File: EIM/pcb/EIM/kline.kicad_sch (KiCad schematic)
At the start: 8 parts, among them IC1 TLIN1027DRQ1

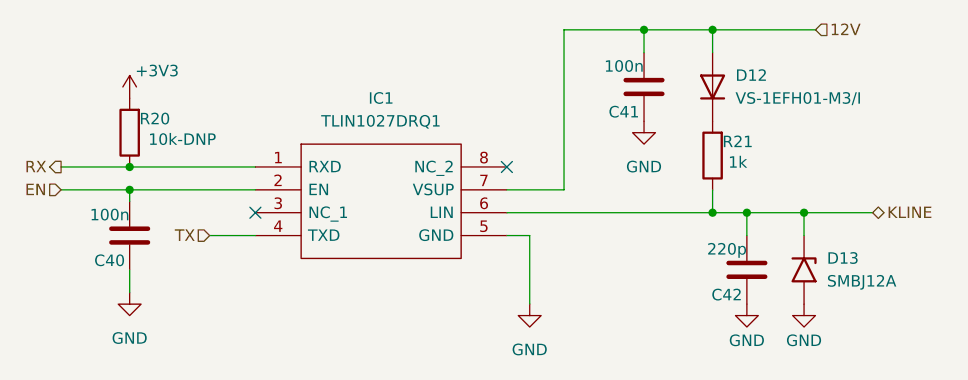
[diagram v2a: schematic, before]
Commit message: All components placed and pins assigned.
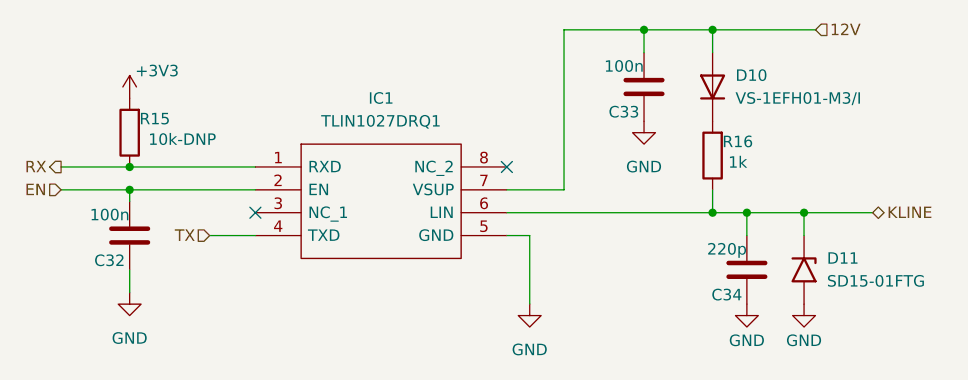
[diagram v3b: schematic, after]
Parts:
- removed D13: SMBJ12A, Diode_SMD:D_SMB, symbol Diode:SM6T10A
- added D11: SD15-01FTG, Diode_SMD:D_SOD-323, symbol Diode:SM6T10A
- renumbered C40 to C32, C41 to C33, C42 to C34, D12 to D10, R20 to R15, R21 to R16
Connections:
- net GND: now also D11.2 (A2)
- net KLINE: now also D11.1 (A1)
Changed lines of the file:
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@@
 		(on_board yes)
 		(dnp no)
-		(property "Reference" "#PWR093"
+		(property "Reference" "#PWR086"
 			(at 186.69 113.03 0)
 			(effects
@@
 			(project "EIM"
 				(path "/2e0b3b3d-5537-41dc-9fad-4fb33afdbfad/08df7d8f-6781-4b98-a316-f1c5c896db59"
-					(reference "#PWR093")
+					(reference "#PWR086")
 					(unit 1)
 				)
@@
 		(dnp no)
 		(fields_autoplaced yes)
-		(property "Reference" "#PWR091"
+		(property "Reference" "#PWR084"
 			(at 162.56 113.03 0)
 			(effects
@@
 			(project ""
 				(path "/2e0b3b3d-5537-41dc-9fad-4fb33afdbfad/08df7d8f-6781-4b98-a316-f1c5c896db59"
-					(reference "#PWR091")
+					(reference "#PWR084")
 					(unit 1)
 				)
@@
 		(on_board yes)
 		(dnp no)
-		(property "Reference" "#PWR089"
+		(property "Reference" "#PWR082"
 			(at 118.11 87.63 0)
 			(effects
@@
 			(project "EIM"
 				(path "/2e0b3b3d-5537-41dc-9fad-4fb33afdbfad/08df7d8f-6781-4b98-a316-f1c5c896db59"
-					(reference "#PWR089")
+					(reference "#PWR082")
 					(unit 1)
 				)
@@
 		(on_board yes)
 		(dnp no)
-		(property "Reference" "C41"
+		(property "Reference" "C33"
 			(at 174.752 85.344 0)
 			(effects
@@
 			(project "EIM"
 				(path "/2e0b3b3d-5537-41dc-9fad-4fb33afdbfad/08df7d8f-6781-4b98-a316-f1c5c896db59"
-					(reference "C41")
+					(reference "C33")
 					(unit 1)
 				)
@@
 		(dnp no)
 		(fields_autoplaced yes)
-		(property "Reference" "#PWR090"
+		(property "Reference" "#PWR083"
 			(at 118.11 111.76 0)
 			(effects
@@
 			(project "EIM"
 				(path "/2e0b3b3d-5537-41dc-9fad-4fb33afdbfad/08df7d8f-6781-4b98-a316-f1c5c896db59"
-					(reference "#PWR090")
+					(reference "#PWR083")
+					(unit 1)
+				)
+			)
+		)
+	)
+	(symbol
+		(lib_id "Diode:SM6T10A")
+		(at 193.04 102.87 270)
+		(unit 1)
+		(exclude_from_sim no)
+		(in_bom yes)
+		(on_board yes)
+		(dnp no)
+		(property "Reference" "D11"
+			(at 195.58 101.5999 90)
+			(effects
+				(font
+					(size 1.27 1.27)
+				)
+				(justify left)
+			)
+		)
+		(property "Value" "SD15-01FTG"
+			(at 195.58 104.1399 90)
+			(effects
+				(font
+					(size 1.27 1.27)
+				)
+				(justify left)
+			)
+		)
+		(property "Footprint" "Diode_SMD:D_SOD-323"
+			(at 187.96 102.87 0)
+			(effects
+				(font
+					(size 1.27 1.27)
+				)
+				(hide yes)
+			)
+		)
+		(property "Datasheet" "https://www.st.com/resource/en/datasheet/sm6t.pdf"
+			(at 193.04 101.6 0)
+			(effects
+				(font
+					(size 1.27 1.27)
+				)
+				(hide yes)
+			)
+		)
+		(property "Description" "600W unidirectional Transil Transient Voltage Suppressor, 10Vrwm, DO-214AA"
+			(at 193.04 102.87 0)
+			(effects
+				(font
+					(size 1.27 1.27)
+				)
+				(hide yes)
+			)
+		)
+		(pin "1"
+		)
+		(pin "2"
+		)
+		(instances
+			(project "EIM"
+				(path "/2e0b3b3d-5537-41dc-9fad-4fb33afdbfad/08df7d8f-6781-4b98-a316-f1c5c896db59"
+					(reference "D11")
 					(unit 1)
 				)
@@
 		(on_board yes)
 		(dnp no)
-		(property "Reference" "C42"
+		(property "Reference" "C34"
 			(at 186.182 105.664 0)
 			(effects
@@
 			(project "EIM"
 				(path "/2e0b3b3d-5537-41dc-9fad-4fb33afdbfad/08df7d8f-6781-4b98-a316-f1c5c896db59"
-					(reference "C42")
-					(unit 1)
-				)
-			)
-		)
-	)
-	(symbol
-		(lib_id "Diode:SM6T10A")
-		(at 193.04 102.87 270)
-		(unit 1)
-		(exclude_from_sim no)
-		(in_bom yes)
-		(on_board yes)
-		(dnp no)
-		(property "Reference" "D13"
-			(at 195.58 101.5999 90)
-			(effects
-				(font
-					(size 1.27 1.27)
-				)
-				(justify left)
-			)
-		)
-		(property "Value" "SMBJ12A"
-			(at 195.58 104.1399 90)
-			(effects
-				(font
-					(size 1.27 1.27)
-				)
-				(justify left)
-			)
-		)
-		(property "Footprint" "Diode_SMD:D_SMB"
-			(at 187.96 102.87 0)
-			(effects
-				(font
-					(size 1.27 1.27)
-				)
-				(hide yes)
-			)
-		)
-		(property "Datasheet" "https://www.st.com/resource/en/datasheet/sm6t.pdf"
-			(at 193.04 101.6 0)
-			(effects
-				(font
-					(size 1.27 1.27)
-				)
-				(hide yes)
-			)
-		)
-		(property "Description" "600W unidirectional Transil Transient Voltage Suppressor, 10Vrwm, DO-214AA"
-			(at 193.04 102.87 0)
-			(effects
-				(font
-					(size 1.27 1.27)
-				)
-				(hide yes)
-			)
-		)
-		(pin "1"
-		)
-		(pin "2"
-		)
-		(instances
-			(project "EIM"
-				(path "/2e0b3b3d-5537-41dc-9fad-4fb33afdbfad/08df7d8f-6781-4b98-a316-f1c5c896db59"
-					(reference "D13")
+					(reference "C34")
 					(unit 1)
 				)
@@
 		(on_board yes)
 		(dnp no)
-		(property "Reference" "R21"
+		(property "Reference" "R16"
 			(at 185.674 88.646 0)
 			(effects
@@
 			(project "EIM"
 				(path "/2e0b3b3d-5537-41dc-9fad-4fb33afdbfad/08df7d8f-6781-4b98-a316-f1c5c896db59"
-					(reference "R21")
+					(reference "R16")
 					(unit 1)
 				)
@@
 		(dnp no)
 		(fields_autoplaced yes)
-		(property "Reference" "D12"
+		(property "Reference" "D10"
 			(at 185.42 81.2799 90)
 			(effects
@@
 			(project ""
 				(path "/2e0b3b3d-5537-41dc-9fad-4fb33afdbfad/08df7d8f-6781-4b98-a316-f1c5c896db59"
-					(reference "D12")
+					(reference "D10")
 					(unit 1)
 				)
@@
 		(on_board yes)
 		(dnp no)
-		(property "Reference" "#PWR094"
+		(property "Reference" "#PWR087"
 			(at 193.04 113.03 0)
 			(effects
@@
 			(project "EIM"
 				(path "/2e0b3b3d-5537-41dc-9fad-4fb33afdbfad/08df7d8f-6781-4b98-a316-f1c5c896db59"
-					(reference "#PWR094")
+					(reference "#PWR087")
 					(unit 1)
 				)
@@
 		(dnp no)
 		(fields_autoplaced yes)
-		(property "Reference" "#PWR092"
+		(property "Reference" "#PWR085"
 			(at 175.26 92.71 0)
 			(effects
@@
 			(project "EIM"
 				(path "/2e0b3b3d-5537-41dc-9fad-4fb33afdbfad/08df7d8f-6781-4b98-a316-f1c5c896db59"
-					(reference "#PWR092")
+					(reference "#PWR085")
 					(unit 1)
 				)
@@
 		(on_board yes)
 		(dnp no)
-		(property "Reference" "C40"
+		(property "Reference" "C32"
 			(at 117.602 101.854 0)
 			(effects
@@
 			(project "EIM"
 				(path "/2e0b3b3d-5537-41dc-9fad-4fb33afdbfad/08df7d8f-6781-4b98-a316-f1c5c896db59"
-					(reference "C40")
+					(reference "C32")
 					(unit 1)
 				)
@@
 		(on_board yes)
 		(dnp no)
-		(property "Reference" "R20"
+		(property "Reference" "R15"
 			(at 120.904 86.106 0)
 			(effects
@@
 			(project "EIM"
 				(path "/2e0b3b3d-5537-41dc-9fad-4fb33afdbfad/08df7d8f-6781-4b98-a316-f1c5c896db59"
-					(reference "R20")
-					(unit 1)
-				)
+					(reference "R15")
+					(unit 1)
+				)
